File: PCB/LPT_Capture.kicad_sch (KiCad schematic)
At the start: 12 parts, among them J1 USB3155-XX-X_REVA, J2 DB25 Male, U1 FT245RL

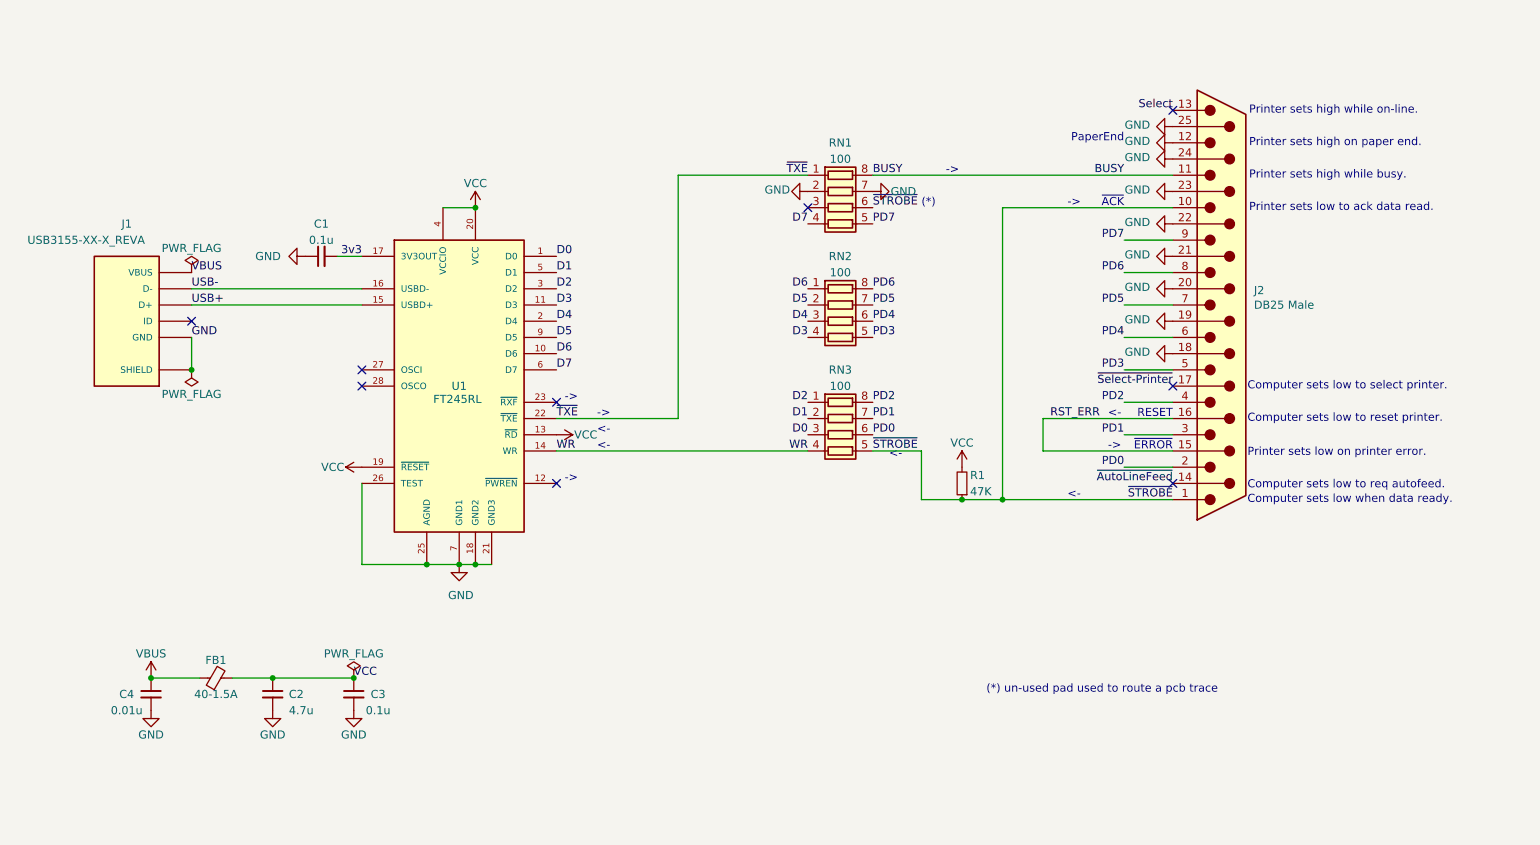
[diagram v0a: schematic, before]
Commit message: minor routing and silkscreen touch ups
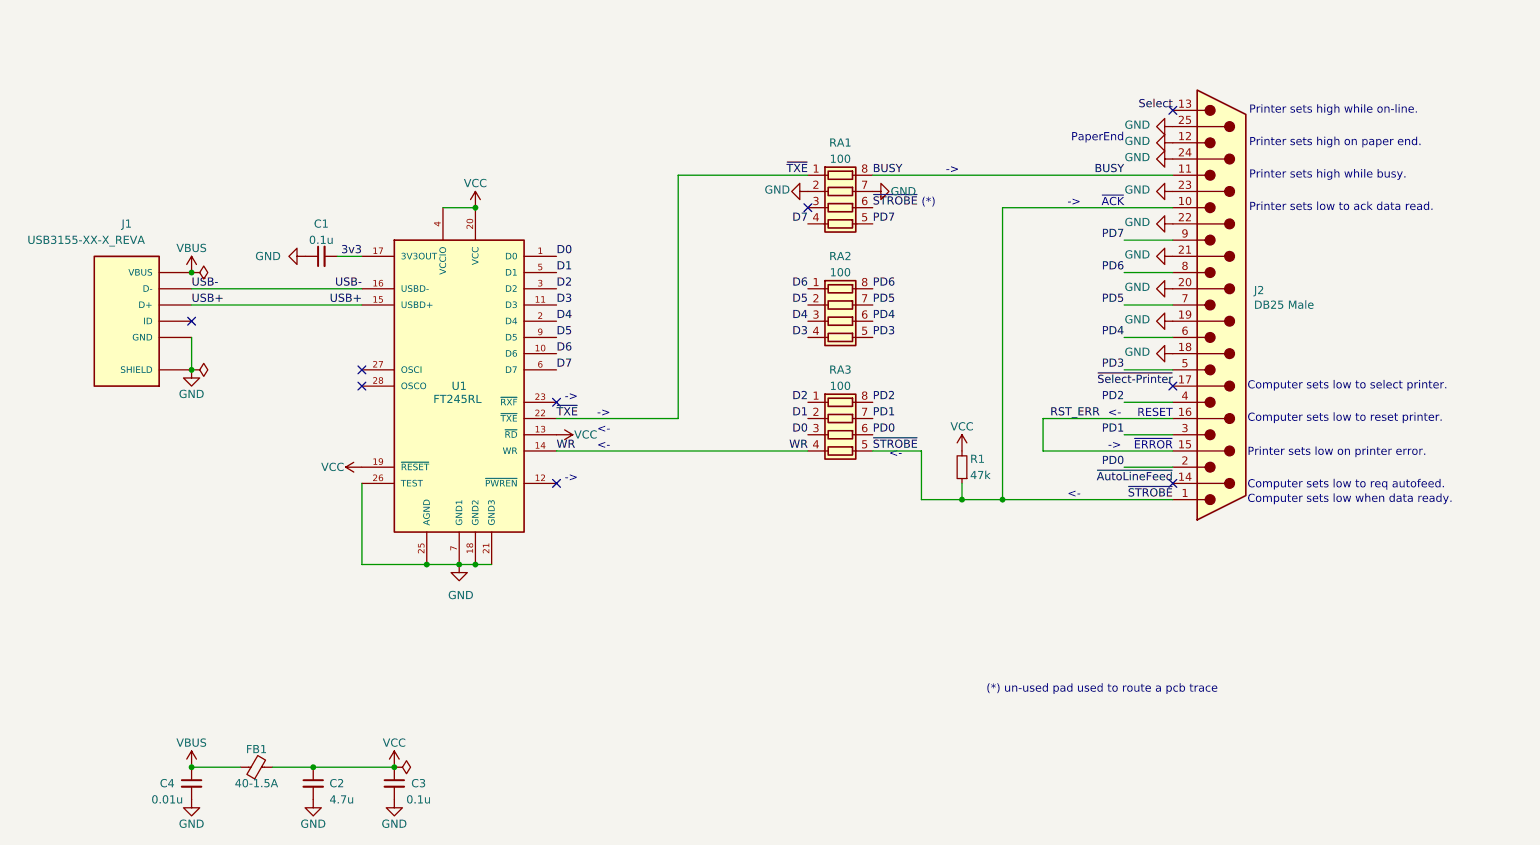
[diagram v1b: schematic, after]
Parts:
- R1: value 47K -> 47k
- renumbered RN1 to RA1, RN2 to RA2, RN3 to RA3
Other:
- moved on the sheet: C2, C3, C4, FB1, R1

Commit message: add ONLINE & /RESET
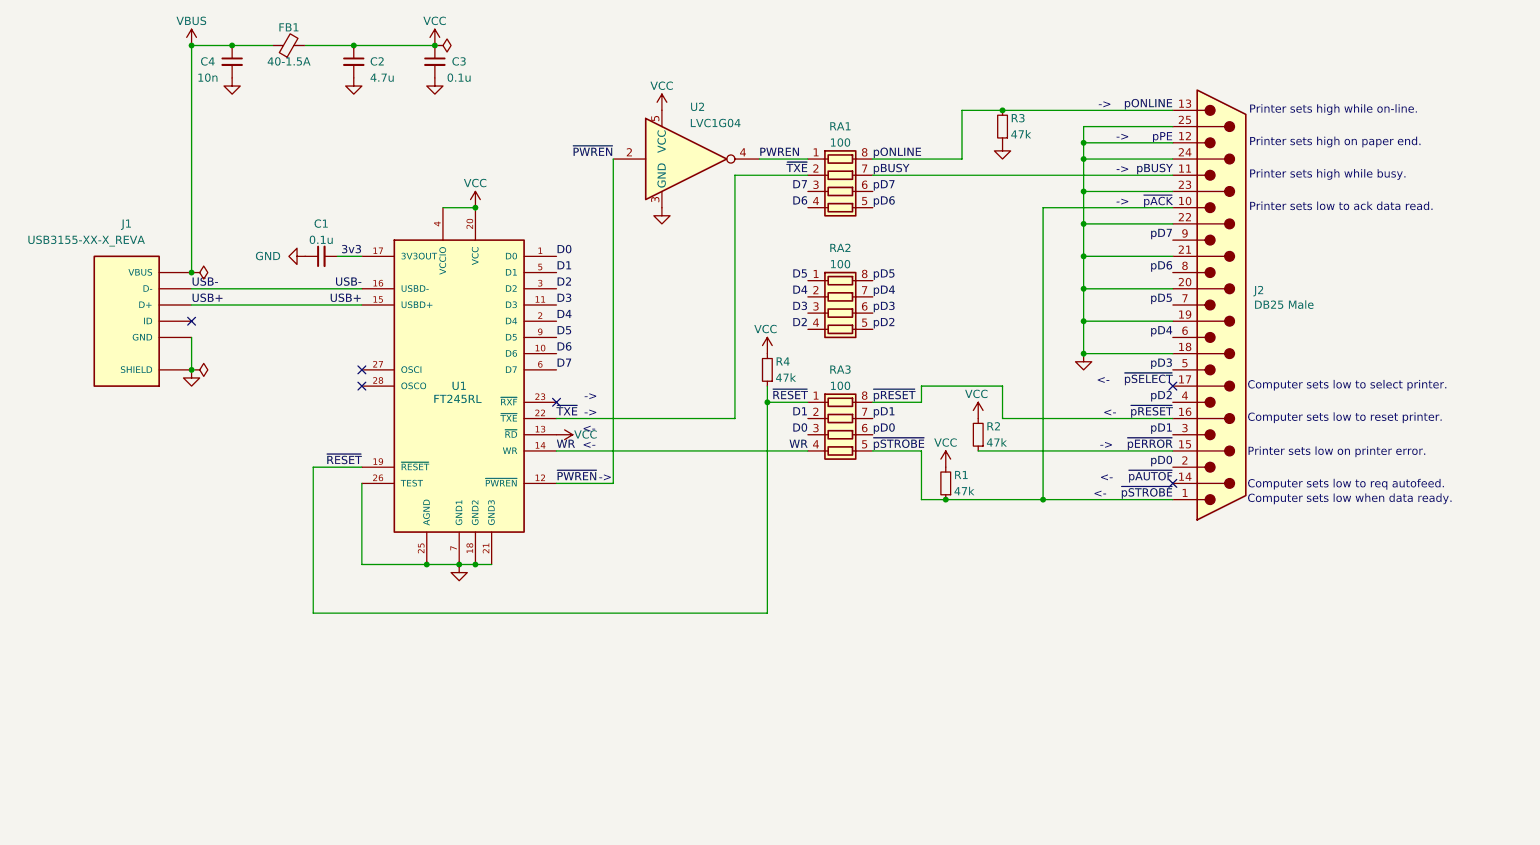
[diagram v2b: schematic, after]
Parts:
- added R2, R3, R4: 47k, 000_LOCAL:R_0805_2012Metric, symbol 000_LOCAL:R_Small
- added U2: LVC1G04, 000_LOCAL:SOT-353_SC-70-5, symbol 000_LOCAL:74LVC1G04
- C4: value 0.01u -> 10n
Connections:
- net D2: now also RA2.4 (R4.1); no longer RA3.1 (R1.1)
- net D3: now also RA2.3 (R3.1); no longer RA2.4 (R4.1)
- net D4: now also RA2.2 (R2.1); no longer RA2.3 (R3.1)
- net D5: now also RA2.1 (R1.1); no longer RA2.2 (R2.1)
- net D6: now also RA1.4 (R4.1); no longer RA2.1 (R1.1)
- net D7: now also RA1.3 (R3.1); no longer RA1.4 (R4.1)
- net GND: now also R3.1, U2.3 (GND); no longer RA1.2 (R2.1), RA1.7 (R2.2)
- net VCC: now also R2.2, R4.2, U2.5 (VCC); no longer U1.19 (~{RESET})
- net ~{TXE}: now also RA1.2 (R2.1); no longer RA1.1 (R1.1)
- net ~{PWREN}: now reaches U1.12 (~{PWREN})
- net ~{PWREN}: now also U2.2
- net BUSY renamed pBUSY
- net pBUSY: now also RA1.7 (R2.2); no longer RA1.8 (R1.2)
- net PD0 renamed pD0
- net PD1 renamed pD1
- net PD2 renamed pD2
- net pD2: now also RA2.5 (R4.2); no longer RA3.8 (R1.2)
- net PD3 renamed pD3
- net pD3: now also RA2.6 (R3.2); no longer RA2.5 (R4.2)
- net PD4 renamed pD4
- net pD4: now also RA2.7 (R2.2); no longer RA2.6 (R3.2)
- net PD5 renamed pD5
- net pD5: now also RA2.8 (R1.2); no longer RA2.7 (R2.2)
- net PD6 renamed pD6
- net pD6: now also RA1.5 (R4.2); no longer RA2.8 (R1.2)
- net PD7 renamed pD7
- net pD7: now also RA1.6 (R3.2); no longer RA1.5 (R4.2)
- net RST_ERR renamed ~{pERROR}
- net ~{pERROR}: now also R2.1; no longer J2.16 (P16)
- net Select renamed pONLINE
- net pONLINE: now also RA1.8 (R1.2), R3.2
- net ~{AutoLineFeed} renamed ~{pAUTOF}
- net ~{STROBE} renamed ~{pSTROBE}
- net ~{pSTROBE}: no longer RA1.6 (R3.2)
- net ~{Select-Printer} renamed ~{pSELECT}
- new net PWREN: RA1.1 (R1.1), U2.4
- new net ~{RESET}: R4.1, RA3.1 (R1.1), U1.19 (~{RESET})
- new net ~{pRESET}: J2.16 (P16), RA3.8 (R1.2)
- no-connect marks 9 -> 6
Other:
- note added: "pPE"
- note added: "~{pACK}"
- note removed: "(*)"
- note removed: "(*) un-used pad used to route a pcb trace"
- note removed: "PaperEnd"
- note removed: "RESET"
- note removed: "~{ACK}"
- note removed: "~{ERROR}"
- moved on the sheet: C2, C3, C4, FB1, R1, RA1, RA2
